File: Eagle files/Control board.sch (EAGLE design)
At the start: 27 parts

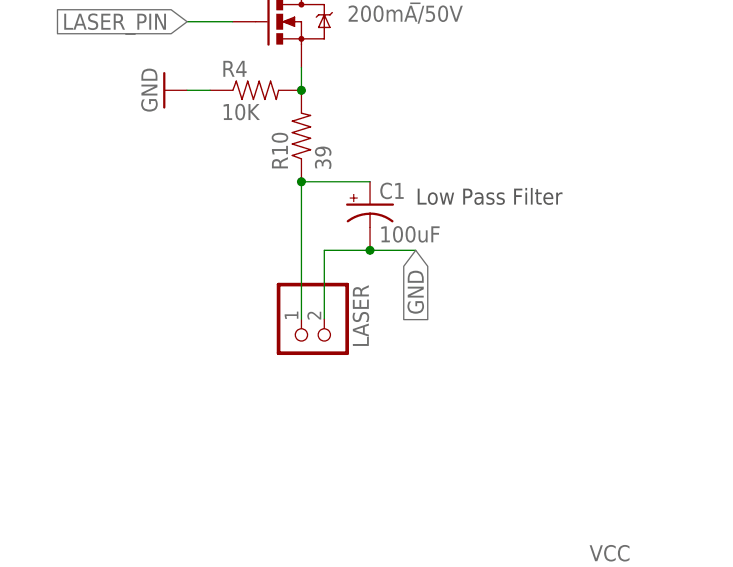
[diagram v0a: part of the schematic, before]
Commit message: added reverse diode protection on laser
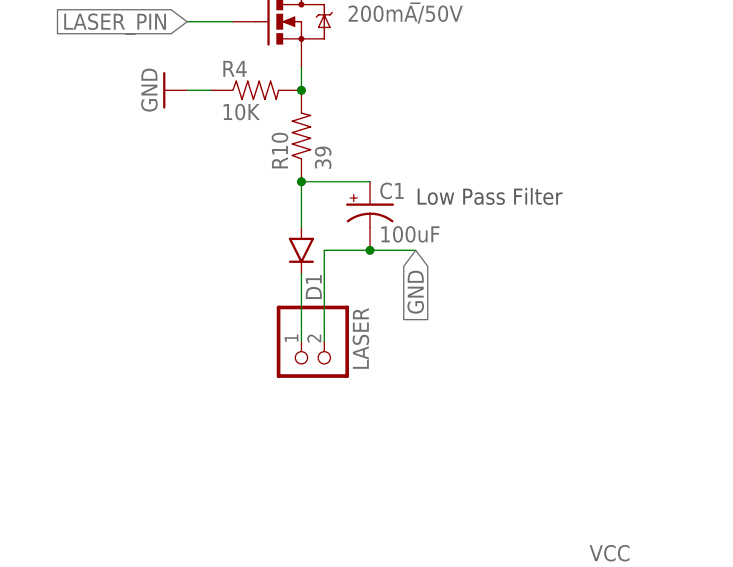
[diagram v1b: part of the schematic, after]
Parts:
- added D1: (no value), SparkFun-DiscreteSemi:DIODESOD123
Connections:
- new net N$2: D1.C, LASER.2
- net N$1: now also D1.A; no longer LASER.2
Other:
- moved on the sheet: LASER
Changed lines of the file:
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@@
 <part name="R10" library="SparkFun-Resistors" deviceset="10KOHM-1/10W-1%(0603)" device="0603" value="39"/>
 <part name="C1" library="SparkFun-Capacitors" deviceset="100UF-10V-10%(TANT)" device="" value="100uF"/>
+<part name="D1" library="SparkFun-DiscreteSemi" deviceset="DIODE" device="SOD123"/>
 </parts>
 <sheets>
@@
 <text x="254" y="60.96" size="2.54" layer="150">-&gt; LEDS</text>
 <text x="73.66" y="165.1" size="2.54" layer="150" align="bottom-right">10K Potentiometer -&gt;</text>
-<text x="48.26" y="106.68" size="2.54" layer="150">-&gt;LASER DIODE</text>
+<text x="58.42" y="106.68" size="2.54" layer="150">-&gt;LASER DIODE</text>
 <text x="50.8" y="124.46" size="1.778" layer="97">Low Pass Filter</text>
 </plain>
@@
 <instance part="X_SERVO" gate="A" x="71.12" y="48.26" rot="R90"/>
 <instance part="Y_SERVO" gate="A" x="104.14" y="43.18" rot="R270"/>
-<instance part="LASER" gate="G$1" x="38.1" y="109.22" rot="R270"/>
+<instance part="LASER" gate="G$1" x="38.1" y="106.68" rot="R270"/>
 <instance part="RUN_MOS" gate="G$1" x="220.98" y="177.8"/>
 <instance part="INT_MOS" gate="G$1" x="220.98" y="142.24"/>
@@
 <instance part="R10" gate="G$1" x="38.1" y="132.08" rot="R90"/>
 <instance part="C1" gate="G$1" x="45.72" y="124.46"/>
+<instance part="D1" gate="G$1" x="38.1" y="119.38" rot="R270"/>
 </instances>
 <busses>
@@
 <segment>
 <pinref part="LASER" gate="G$1" pin="1"/>
-<wire x1="40.64" y1="111.76" x2="40.64" y2="119.38" width="0.1524" layer="91"/>
+<wire x1="40.64" y1="109.22" x2="40.64" y2="119.38" width="0.1524" layer="91"/>
 <wire x1="40.64" y1="119.38" x2="45.72" y2="119.38" width="0.1524" layer="91"/>
 <label x="50.8" y="119.38" size="1.778" layer="95" rot="R270" xref="yes"/>
@@
 <segment>
 <pinref part="R10" gate="G$1" pin="1"/>
-<pinref part="LASER" gate="G$1" pin="2"/>
-<wire x1="38.1" y1="127" x2="38.1" y2="111.76" width="0.1524" layer="91"/>
+<wire x1="38.1" y1="127" x2="38.1" y2="121.92" width="0.1524" layer="91"/>
 <pinref part="C1" gate="G$1" pin="+"/>
 <wire x1="45.72" y1="127" x2="38.1" y2="127" width="0.1524" layer="91"/>
 <junction x="38.1" y="127"/>
+<pinref part="D1" gate="G$1" pin="A"/>
 </segment>
 </net>
@@
 </segment>
 </net>
+<net name="N$2" class="0">
+<segment>
+<pinref part="LASER" gate="G$1" pin="2"/>
+<pinref part="D1" gate="G$1" pin="C"/>
+<wire x1="38.1" y1="116.84" x2="38.1" y2="109.22" width="0.1524" layer="91"/>
+</segment>
+</net>
